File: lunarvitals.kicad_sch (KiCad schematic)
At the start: 38 parts, among them J1 ConductiveCord, J2 MPU6050, J3 SEN11574, J5 USB_C_Receptacle_PowerOnly_6P, J6 Battery, Q1 FS8205A, U1 NRF52840-DONGLE, U2 BMP280, U3 AP2112K-3.3, U4 TP4056, U5 MLX90614ESF-AAA-000-TU, U6 DW01A

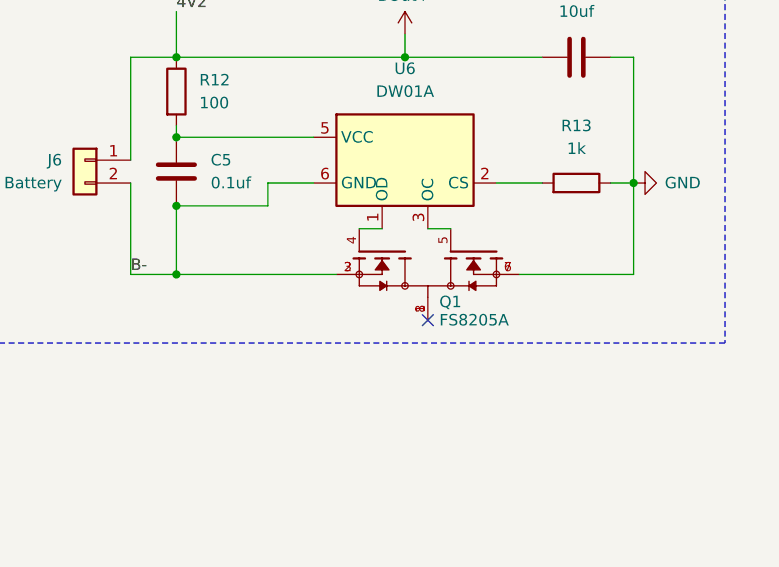
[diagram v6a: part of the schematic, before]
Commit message: fixed out of stock fs8205 and other small fixes
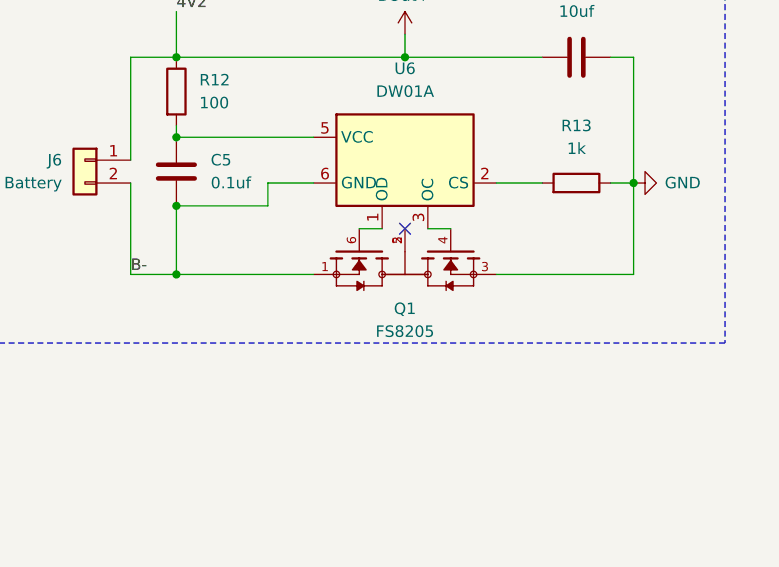
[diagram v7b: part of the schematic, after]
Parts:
- removed Q1: FS8205A, FS8205A:SOP65P640X120-8N, symbol FS8205A:FS8205A
- added Q1: FS8205, FS8205A:SOT95P280X145-6N, symbol FS8205A:FS8205
- J5: LCSC (none) -> C668623
- U4: LCSC (none) -> C16581
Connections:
- net B-: now also Q1.1
- net GND: now also Q1.3
- net at U6.1 (OD): now also Q1.6
- net at U6.3 (OC): now also Q1.4
- new net: Q1.2, Q1.5

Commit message: LCSC part numbers
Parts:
- J1: LCSC (none) -> C158012
- J2: LCSC C491709 -> C144395
- J3: LCSC C265055 -> C144394
- J6: LCSC (none) -> C160402
- Q1: Description_1 Dual N-Channel Enhancement Mode Power MOSFET -> (none); LCSC (none) -> C908265; MANUFACTURER Fortune -> (none); Price None -> (none)
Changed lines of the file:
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@@
 			)
 		)
+		(property "LCSC" "C158012"
+			(at 96.52 180.34 0)
+			(effects
+				(font
+					(size 1.27 1.27)
+				)
+				(hide yes)
+			)
+		)
 		(pin "2"
 		)
@@
 			)
 		)
-		(property "LCSC" "C491709"
+		(property "LCSC" "C144395"
 			(at 38.1 180.34 0)
 			(effects
@@
 			)
 		)
+		(property "LCSC" "C160402"
+			(at 189.23 143.51 0)
+			(effects
+				(font
+					(size 1.27 1.27)
+				)
+				(hide yes)
+			)
+		)
 		(pin "2"
 		)
@@
 			)
 		)
-		(property "Price" "None"
-			(at 224.79 156.21 0)
-			(effects
-				(font
-					(size 1.27 1.27)
-				)
-				(justify bottom)
-				(hide yes)
-			)
-		)
 		(property "Check_prices" "https://www.snapeda.com/parts/FS8205/Fortune+Semiconductor/view-part/?ref=eda"
 			(at 224.79 156.21 0)
@@
 			)
 		)
-		(property "Description_1" "\n                        \n                            Dual N-Channel Enhancement Mode Power MOSFET\n                        \n"
-			(at 224.79 156.21 0)
-			(effects
-				(font
-					(size 1.27 1.27)
-				)
-				(justify bottom)
-				(hide yes)
-			)
-		)
 		(property "Availability" "In Stock"
 			(at 224.79 156.21 0)
@@
 			)
 		)
-		(property "MANUFACTURER" "Fortune"
-			(at 224.79 156.21 0)
+		(property "LCSC" "C908265"
+			(at 224.79 156.21 90)
 			(effects
 				(font
 					(size 1.27 1.27)
 				)
-				(justify bottom)
 				(hide yes)
 			)
@@
 			)
 		)
-		(property "LCSC" "C265055"
+		(property "LCSC" "C144394"
 			(at 96.52 161.29 0)
 			(effects
